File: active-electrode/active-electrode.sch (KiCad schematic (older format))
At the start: 13 parts, among them P1 CONN_1, P2 CONN_1, P3 CONN_1, P4 CONN_1, P5 CONN_1, P6 CONN_1, P7 CONN_1, U1 TLC272

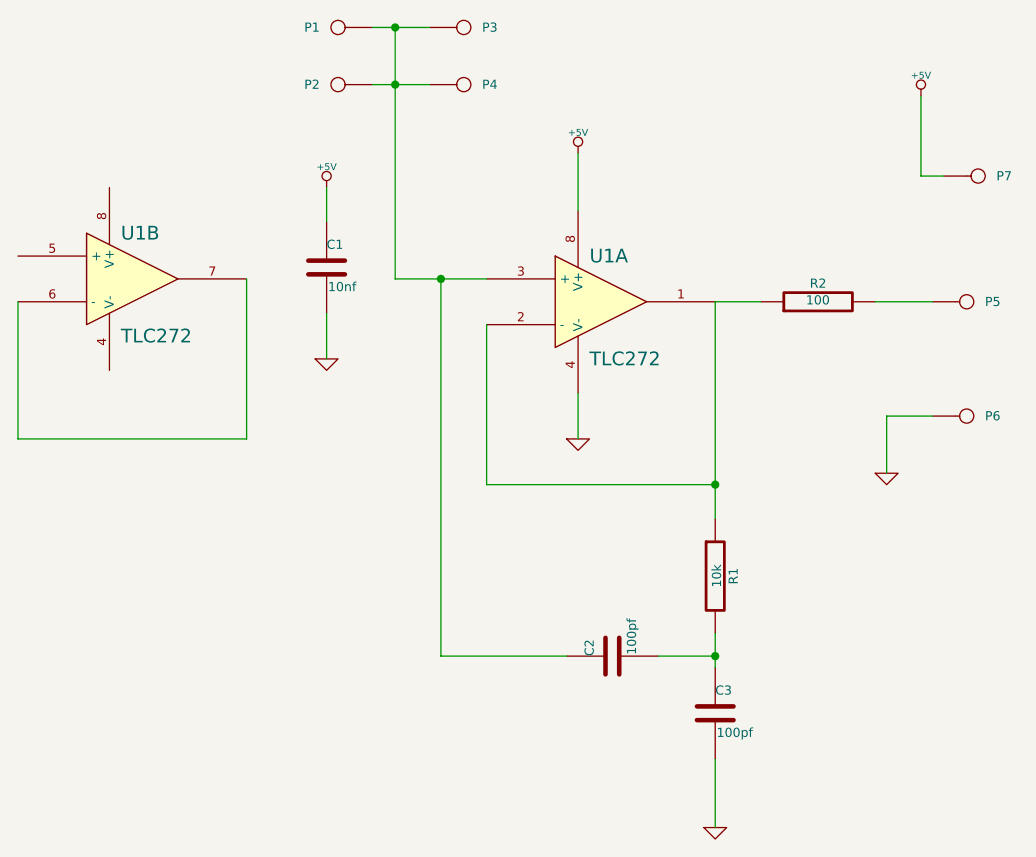
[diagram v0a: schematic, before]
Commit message: fixed diodes on amplifier pcb
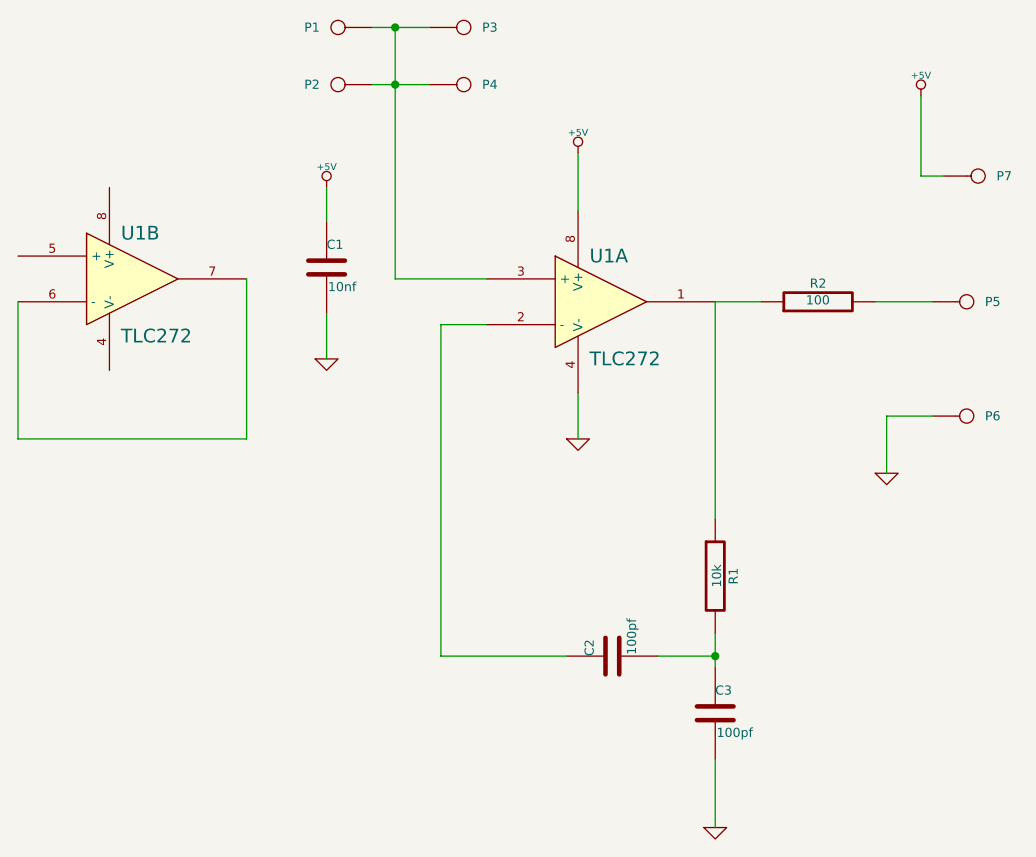
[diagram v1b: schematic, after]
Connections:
- net at R1.1, R2.1, U1.1: no longer U1.2 (-)
- net at P1.1, P2.1, P3.1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: no longer C2.1
- new net: C2.1, U1.2 (-)
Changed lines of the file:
@@
 Sheet 1 1
 Title ""
-Date "17 jul 2015"
+Date "1 feb 2016"
 Rev ""
 Comp ""
@@
 $EndComp
 $Comp
+L CONN_1 P4
+U 1 1 5592EFD8
+P 3000 1500
+F 0 "P4" H 3080 1500 40  0000 L CNN
+F 1 "CONN_1" H 3000 1555 30  0001 C CNN
+F 2 "" H 3000 1500 60  0000 C CNN
+F 3 "" H 3000 1500 60  0000 C CNN
+	1    3000 1500
+	1    0    0    -1
+$EndComp
+$Comp
+L CONN_1 P3
+U 1 1 5592EFF6
+P 3000 1250
+F 0 "P3" H 3080 1250 40  0000 L CNN
+F 1 "CONN_1" H 3000 1305 30  0001 C CNN
+F 2 "" H 3000 1250 60  0000 C CNN
+F 3 "" H 3000 1250 60  0000 C CNN
+	1    3000 1250
+	1    0    0    -1
+$EndComp
+$Comp
+L GND #PWR06
+U 1 1 5592F0F6
+P 4850 3200
+F 0 "#PWR06" H 4850 3200 30  0001 C CNN
+F 1 "GND" H 4850 3130 30  0001 C CNN
+F 2 "" H 4850 3200 60  0000 C CNN
+F 3 "" H 4850 3200 60  0000 C CNN
+	1    4850 3200
+	1    0    0    -1
+$EndComp
+$Comp
+L +5V #PWR07
+U 1 1 5592F105
+P 5000 1550
+F 0 "#PWR07" H 5000 1640 20  0001 C CNN
+F 1 "+5V" H 5000 1640 30  0000 C CNN
+F 2 "" H 5000 1550 60  0000 C CNN
+F 3 "" H 5000 1550 60  0000 C CNN
+	1    5000 1550
+	1    0    0    -1
+$EndComp
+Wire Wire Line
+	3500 2050 3500 1800
+Wire Wire Line
+	3500 2850 3500 3050
+Wire Wire Line
+	2050 2350 2050 3050
+Wire Wire Line
+	2050 3050 1050 3050
+Wire Wire Line
+	1050 3050 1050 2450
+Wire Wire Line
+	4100 3900 4100 4050
+Wire Wire Line
+	4100 4450 4100 4750
+Wire Wire Line
+	3850 4000 4100 4000
+Connection ~ 4100 4000
+Wire Wire Line
+	2400 2700 2400 2500
+Wire Wire Line
+	2400 2100 2400 1950
+Wire Wire Line
+	3450 4000 2900 4000
+Wire Wire Line
+	2700 2350 3100 2350
+Wire Wire Line
+	5050 2950 4850 2950
+Wire Wire Line
+	4850 2950 4850 3200
+Wire Wire Line
+	5100 1900 5000 1900
+Wire Wire Line
+	5000 1900 5000 1550
+$Comp
+L CONN_1 P5
+U 1 1 55931154
+P 5200 2450
+F 0 "P5" H 5280 2450 40  0000 L CNN
+F 1 "CONN_1" H 5200 2505 30  0001 C CNN
+F 2 "" H 5200 2450 60  0000 C CNN
+F 3 "" H 5200 2450 60  0000 C CNN
+	1    5200 2450
+	1    0    0    -1
+$EndComp
+$Comp
+L CONN_1 P7
+U 1 1 55931163
+P 5250 1900
+F 0 "P7" H 5330 1900 40  0000 L CNN
+F 1 "CONN_1" H 5250 1955 30  0001 C CNN
+F 2 "" H 5250 1900 60  0000 C CNN
+F 3 "" H 5250 1900 60  0000 C CNN
+	1    5250 1900
+	1    0    0    -1
+$EndComp
+$Comp
+L CONN_1 P6
+U 1 1 55931172
+P 5200 2950
+F 0 "P6" H 5280 2950 40  0000 L CNN
+F 1 "CONN_1" H 5200 3005 30  0001 C CNN
+F 2 "" H 5200 2950 60  0000 C CNN
+F 3 "" H 5200 2950 60  0000 C CNN
+	1    5200 2950
+	1    0    0    -1
+$EndComp
+Wire Wire Line
+	4800 2450 5050 2450
+Connection ~ 2700 1250
+Connection ~ 2700 1500
+Wire Wire Line
+	2700 1250 2700 2350
+Wire Wire Line
+	2600 1500 2850 1500
+Wire Wire Line
+	2600 1250 2850 1250
+$Comp
+L CONN_1 P1
+U 1 1 5592EFE7
+P 2450 1250
+F 0 "P1" H 2530 1250 40  0000 L CNN
+F 1 "CONN_1" H 2450 1305 30  0001 C CNN
+F 2 "" H 2450 1250 60  0000 C CNN
+F 3 "" H 2450 1250 60  0000 C CNN
+	1    2450 1250
+	-1   0    0    -1
+$EndComp
+$Comp
 L CONN_1 P2
 U 1 1 5592EFC9
@@
 	-1   0    0    1
 $EndComp
-$Comp
-L CONN_1 P4
-U 1 1 5592EFD8
-P 3000 1500
-F 0 "P4" H 3080 1500 40  0000 L CNN
-F 1 "CONN_1" H 3000 1555 30  0001 C CNN
-F 2 "" H 3000 1500 60  0000 C CNN
-F 3 "" H 3000 1500 60  0000 C CNN
-	1    3000 1500
-	1    0    0    -1
-$EndComp
-$Comp
-L CONN_1 P1
-U 1 1 5592EFE7
-P 2450 1250
-F 0 "P1" H 2530 1250 40  0000 L CNN
-F 1 "CONN_1" H 2450 1305 30  0001 C CNN
-F 2 "" H 2450 1250 60  0000 C CNN
-F 3 "" H 2450 1250 60  0000 C CNN
-	1    2450 1250
-	-1   0    0    -1
-$EndComp
-$Comp
-L CONN_1 P3
-U 1 1 5592EFF6
-P 3000 1250
-F 0 "P3" H 3080 1250 40  0000 L CNN
-F 1 "CONN_1" H 3000 1305 30  0001 C CNN
-F 2 "" H 3000 1250 60  0000 C CNN
-F 3 "" H 3000 1250 60  0000 C CNN
-	1    3000 1250
-	1    0    0    -1
-$EndComp
-$Comp
-L GND #PWR06
-U 1 1 5592F0F6
-P 4850 3200
-F 0 "#PWR06" H 4850 3200 30  0001 C CNN
-F 1 "GND" H 4850 3130 30  0001 C CNN
-F 2 "" H 4850 3200 60  0000 C CNN
-F 3 "" H 4850 3200 60  0000 C CNN
-	1    4850 3200
-	1    0    0    -1
-$EndComp
-$Comp
-L +5V #PWR07
-U 1 1 5592F105
-P 5000 1550
-F 0 "#PWR07" H 5000 1640 20  0001 C CNN
-F 1 "+5V" H 5000 1640 30  0000 C CNN
-F 2 "" H 5000 1550 60  0000 C CNN
-F 3 "" H 5000 1550 60  0000 C CNN
-	1    5000 1550
-	1    0    0    -1
-$EndComp
-Wire Wire Line
-	3500 2050 3500 1800
-Wire Wire Line
-	3500 2850 3500 3050
-Wire Wire Line
-	3100 2550 3100 3250
-Wire Wire Line
-	3100 3250 4100 3250
-Wire Wire Line
-	4100 2450 4100 3400
-Wire Wire Line
-	2050 2350 2050 3050
-Wire Wire Line
-	2050 3050 1050 3050
-Wire Wire Line
-	1050 3050 1050 2450
-Connection ~ 4100 3250
-Wire Wire Line
-	4100 3900 4100 4050
-Wire Wire Line
-	4100 4450 4100 4750
-Wire Wire Line
-	3850 4000 4100 4000
-Connection ~ 4100 4000
-Wire Wire Line
-	2400 2700 2400 2500
-Wire Wire Line
-	2400 2100 2400 1950
-Wire Wire Line
-	3450 4000 2900 4000
-Wire Wire Line
-	2900 4000 2900 2350
-Wire Wire Line
-	2700 2350 3100 2350
-Wire Wire Line
-	2600 1250 2850 1250
-Wire Wire Line
-	2600 1500 2850 1500
-Wire Wire Line
-	2700 1250 2700 2350
-Connection ~ 2700 1500
-Connection ~ 2700 1250
-Connection ~ 2900 2350
+Wire Wire Line
+	2900 4000 2900 2550
+Wire Wire Line
+	2900 2550 3100 2550
+Wire Wire Line
+	4100 3400 4100 2450
 Wire Wire Line
 	4100 2450 4300 2450
-Wire Wire Line
-	5050 2950 4850 2950
-Wire Wire Line
-	4850 2950 4850 3200
-Wire Wire Line
-	5100 1900 5000 1900
-Wire Wire Line
-	5000 1900 5000 1550
-$Comp
-L CONN_1 P5
-U 1 1 55931154
-P 5200 2450
-F 0 "P5" H 5280 2450 40  0000 L CNN
-F 1 "CONN_1" H 5200 2505 30  0001 C CNN
-F 2 "" H 5200 2450 60  0000 C CNN
-F 3 "" H 5200 2450 60  0000 C CNN
-	1    5200 2450
-	1    0    0    -1
-$EndComp
-$Comp
-L CONN_1 P7
-U 1 1 55931163
-P 5250 1900
-F 0 "P7" H 5330 1900 40  0000 L CNN
-F 1 "CONN_1" H 5250 1955 30  0001 C CNN
-F 2 "" H 5250 1900 60  0000 C CNN
-F 3 "" H 5250 1900 60  0000 C CNN
-	1    5250 1900
-	1    0    0    -1
-$EndComp
-$Comp
-L CONN_1 P6
-U 1 1 55931172
-P 5200 2950
-F 0 "P6" H 5280 2950 40  0000 L CNN
-F 1 "CONN_1" H 5200 3005 30  0001 C CNN
-F 2 "" H 5200 2950 60  0000 C CNN
-F 3 "" H 5200 2950 60  0000 C CNN
-	1    5200 2950
-	1    0    0    -1
-$EndComp
-Wire Wire Line
-	4800 2450 5050 2450
 $EndSCHEMATC
